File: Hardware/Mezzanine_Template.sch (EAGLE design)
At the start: 10 parts, among them U2 EDISON_CONNECTOR_FULLMOUNTING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, U3 EDISON_CONNECTOR_FULLHEADER

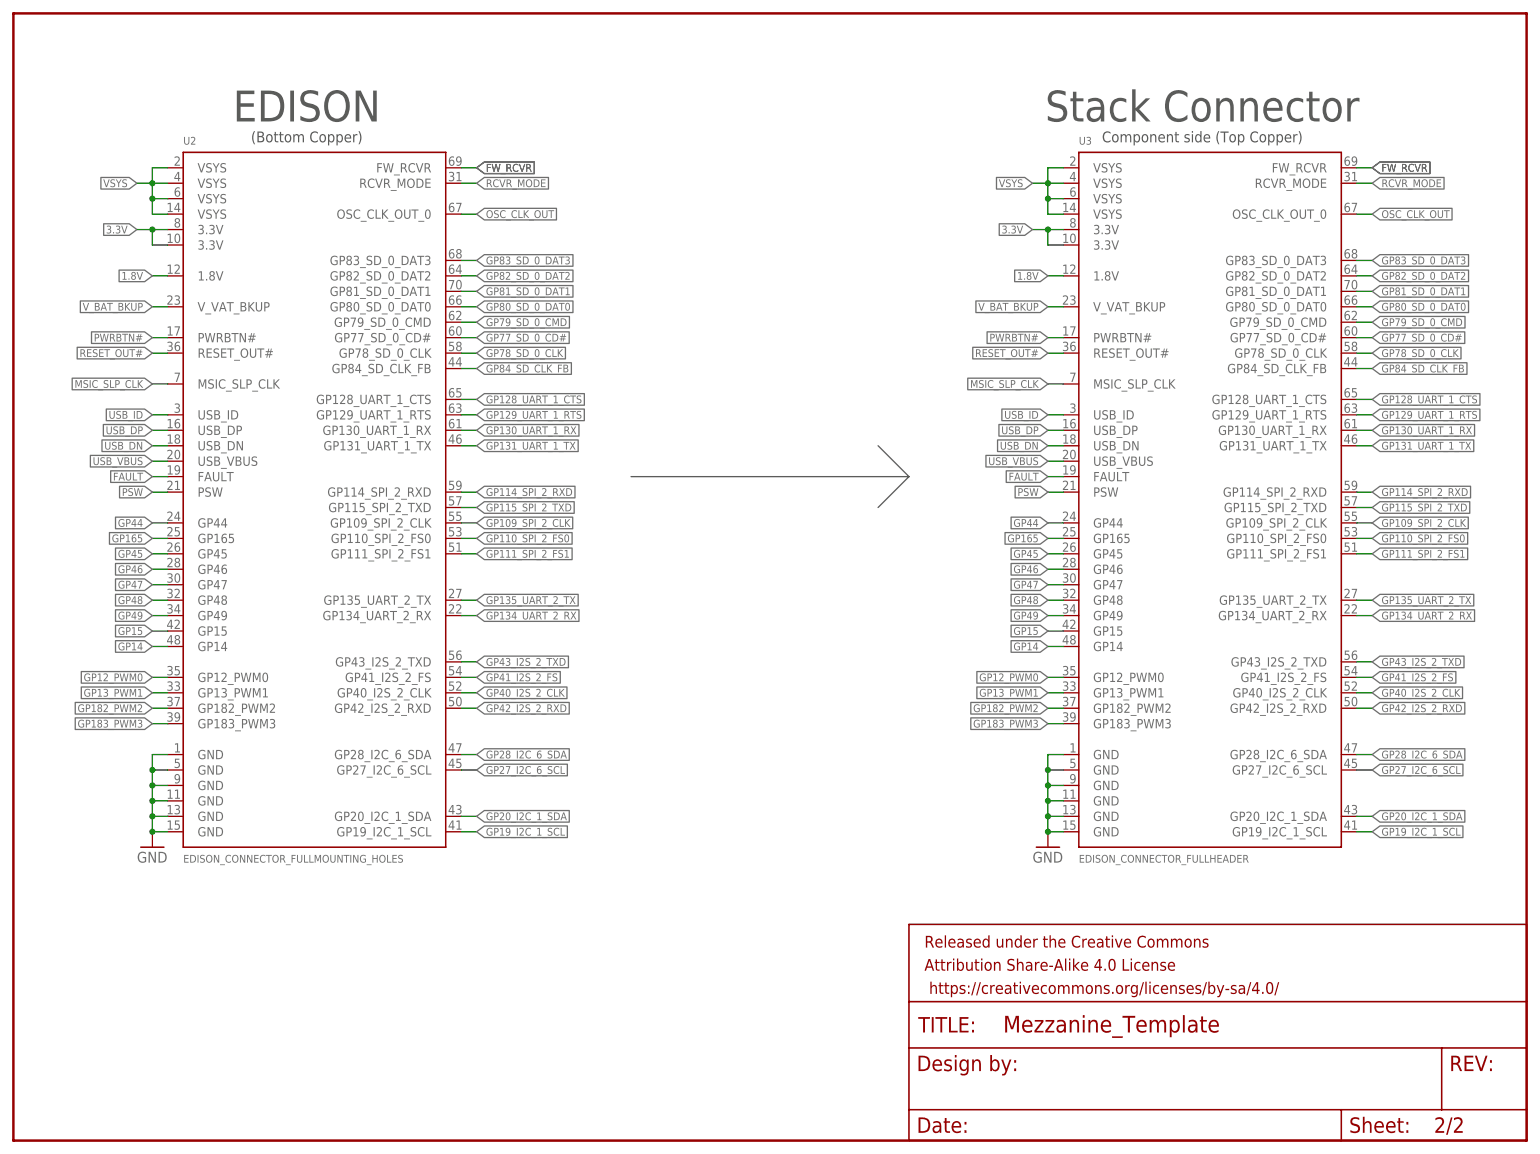
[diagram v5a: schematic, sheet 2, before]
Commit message: clean-up
Board
- Removed duplicate CC frame
- Adjusted sizes, ratios of text so they can be read when "Always Vector
Font" is set
- Adjusted positioning and alignment of text for consistency throughout
the drawing and making the text easier to edit (expansion)
- Fixed corner radius (indicated 0.08", should be 0.07")
- Added unit to the drill hole Dimension as it is -not- in inches
- Fixed top GND plane's bottom right corner (was off a smidgen)
- Centered the SparkFun logos (wiggle wiggle)
- Adjusted version number to 'v01.x' (not for release).  Please make
sure to adjust to appropriate version number before release!

Schematic
- Changed position, ratio and alignment of 'Engineer' in the frame to
align with the rest of the text and be consistent with the board
- Adjusted version number to 'v01.x' (not for release).  Please make
sure to adjust to appropriate version number before release!
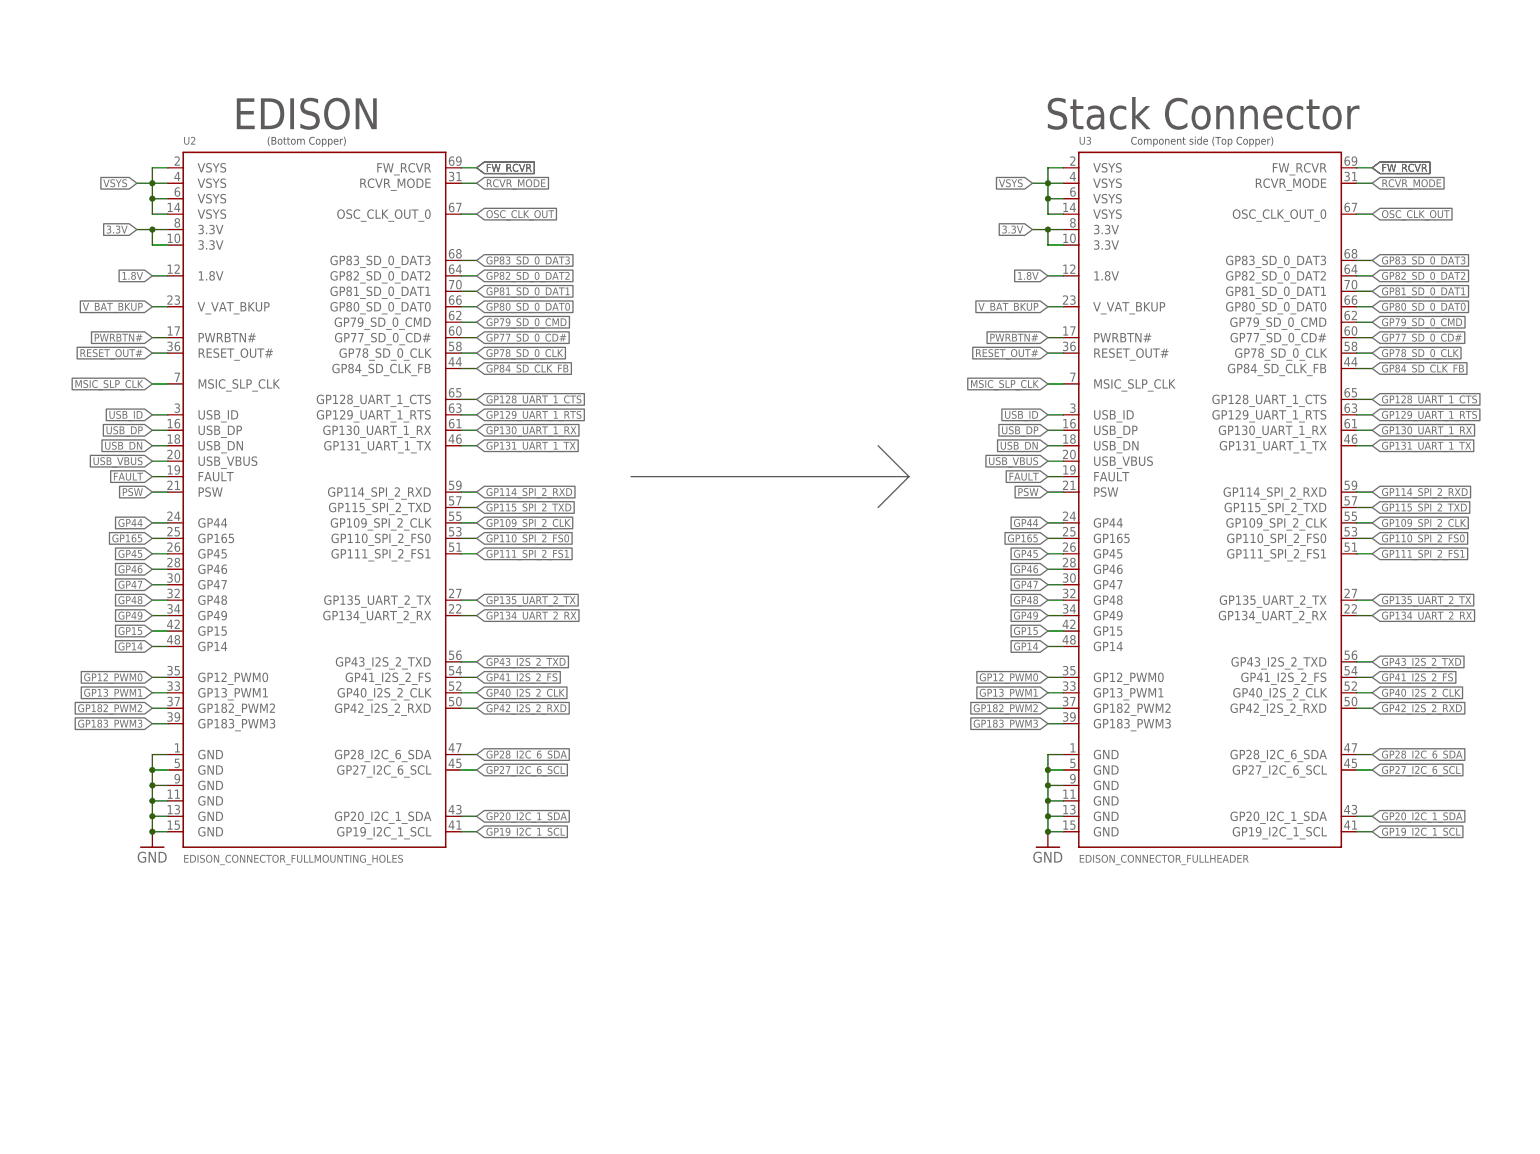
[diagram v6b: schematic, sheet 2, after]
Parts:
- removed FRAME2: FRAME-LETTER, SparkFun-Aesthetics:FRAME-LETTER
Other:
- note added: "v01.x"
- note removed: "v10"
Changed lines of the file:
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@@
 <?xml version="1.0" encoding="utf-8"?>
 <!DOCTYPE eagle SYSTEM "eagle.dtd">
-<eagle version="6.6.0">
+<eagle version="6.5.0">
 <drawing>
 <settings>
@@
 <part name="U3" library="Edison" deviceset="EDISON_CONNECTOR_FULL" device="HEADER" value="EDISON_CONNECTOR_FULLHEADER"/>
 <part name="GND4" library="supply1" deviceset="GND" device=""/>
-<part name="FRAME2" library="SparkFun-Aesthetics" deviceset="FRAME-LETTER" device=""/>
 <part name="FID1" library="SparkFun-Aesthetics" deviceset="FIDUCIAL" device="1X2"/>
 <part name="FID2" library="SparkFun-Aesthetics" deviceset="FIDUCIAL" device="1X2"/>
@@
 <sheet>
 <plain>
-<text x="238.76" y="7.62" size="2.54" layer="94">v10</text>
-<text x="167.64" y="10.16" size="2.54" layer="94">Engineer</text>
+<text x="236.22" y="7.62" size="2.54" layer="94" ratio="15">v01.x</text>
+<text x="172.72" y="13.97" size="2.54" layer="94" ratio="15" align="top-left">Engineer</text>
 </plain>
 <instances>
@@
 <sheet>
 <plain>
-<text x="48.26" y="170.18" size="5.08" layer="92" align="center">EDISON</text>
-<text x="195.58" y="170.18" size="5.08" layer="92" align="center">Stack Connector</text>
-<text x="195.58" y="165.1" size="1.778" layer="92" align="center">Component side (Top Copper)</text>
-<text x="48.26" y="165.1" size="1.778" layer="92" align="center">(Bottom Copper)</text>
+<text x="48.26" y="166.37" size="5.08" layer="92" align="bottom-center">EDISON</text>
+<text x="195.58" y="166.37" size="5.08" layer="92" align="bottom-center">Stack Connector</text>
+<text x="195.58" y="163.83" size="1.27" layer="92" align="bottom-center">Component side (Top Copper)</text>
+<text x="48.26" y="163.83" size="1.27" layer="92" align="bottom-center">(Bottom Copper)</text>
 </plain>
 <instances>
@@
 <instance part="U3" gate="G$1" x="177.8" y="132.08"/>
 <instance part="GND4" gate="1" x="170.18" y="48.26"/>
-<instance part="FRAME2" gate="G$1" x="0" y="0"/>
-<instance part="FRAME2" gate="G$2" x="147.32" y="0"/>
 </instances>
 <busses>

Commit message: replaced some changes made in pull request. updated git ignore to remover .epf
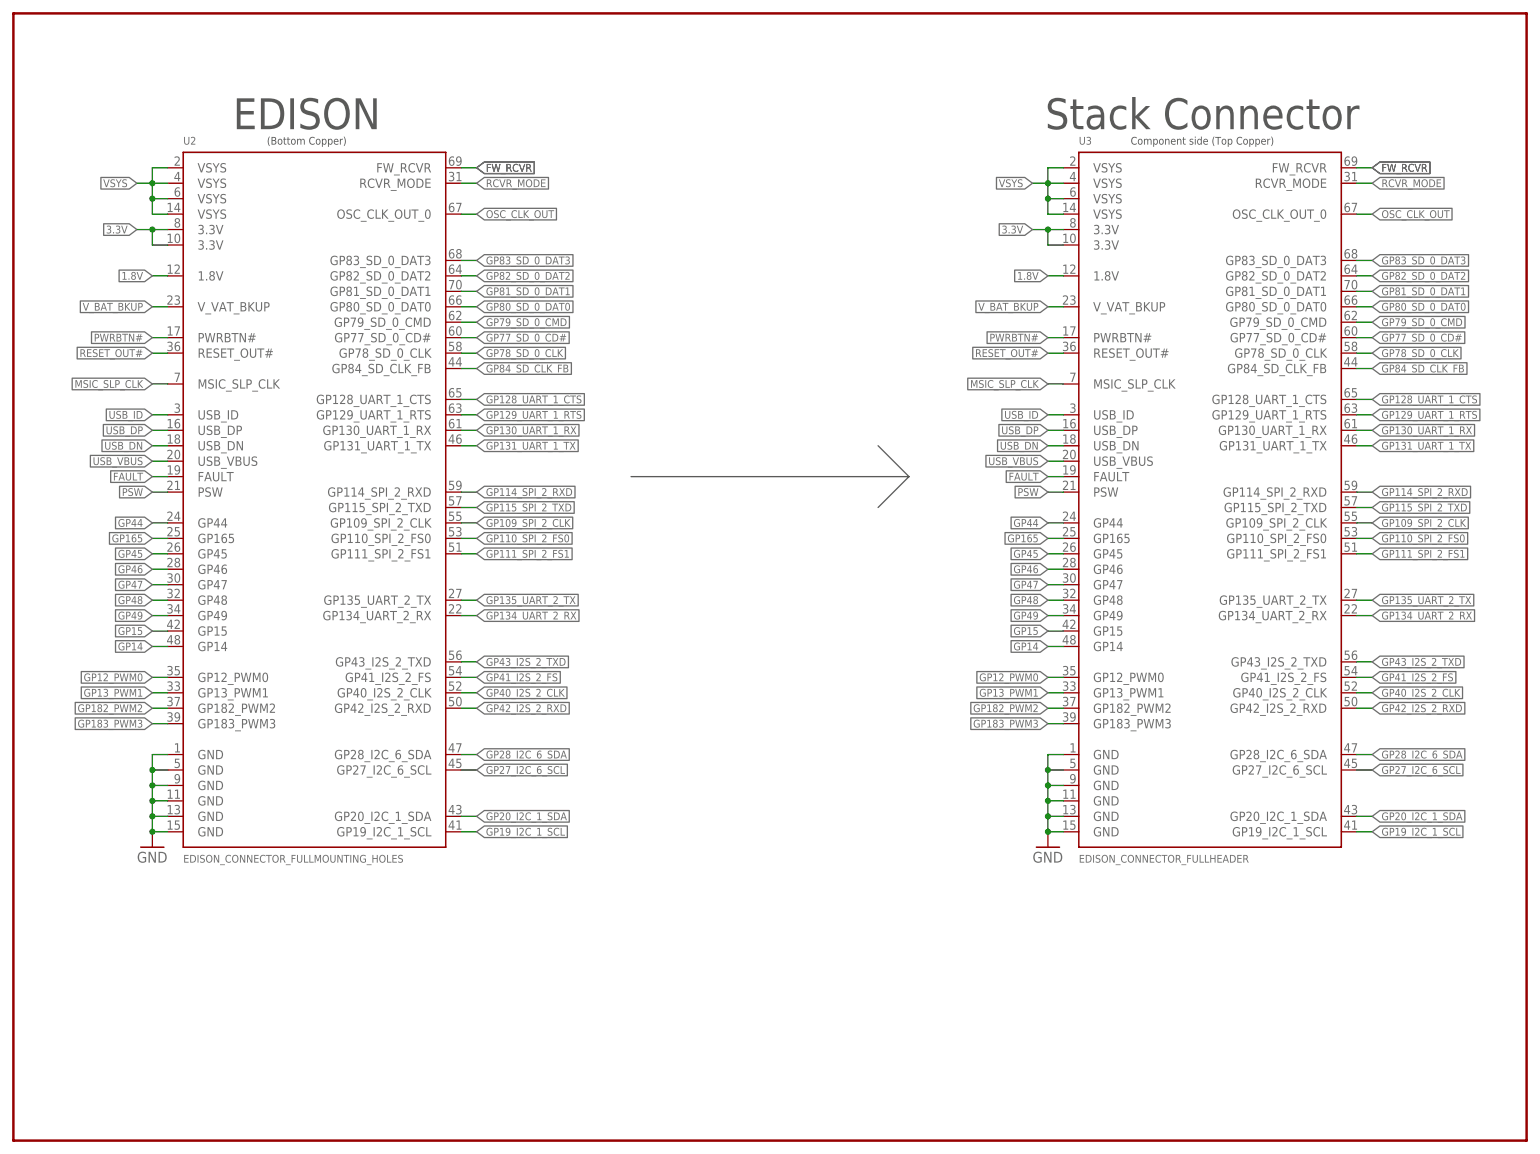
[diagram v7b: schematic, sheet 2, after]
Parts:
- added FRAME2: FRAME-LETTER, SparkFun-Aesthetics:FRAME-LETTER
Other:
- note added: "v01"
- note removed: "v01.x"
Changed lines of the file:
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@@
 <part name="FID3" library="SparkFun-Aesthetics" deviceset="FIDUCIAL" device="1X2"/>
 <part name="FID4" library="SparkFun-Aesthetics" deviceset="FIDUCIAL" device="1X2"/>
+<part name="FRAME2" library="SparkFun-Aesthetics" deviceset="FRAME-LETTER" device=""/>
 </parts>
 <sheets>
 <sheet>
 <plain>
-<text x="236.22" y="7.62" size="2.54" layer="94" ratio="15">v01.x</text>
+<text x="236.22" y="7.62" size="2.54" layer="94" ratio="15">v01</text>
 <text x="172.72" y="13.97" size="2.54" layer="94" ratio="15" align="top-left">Engineer</text>
 </plain>
@@
 <instance part="U3" gate="G$1" x="177.8" y="132.08"/>
 <instance part="GND4" gate="1" x="170.18" y="48.26"/>
+<instance part="FRAME2" gate="G$1" x="0" y="0"/>
 </instances>
 <busses>

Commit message: modified:   Hardware/Edison.lbr 	Corrected DCIN pin name on all schematic drawings
	modified:   Hardware/Mezzanine_Template.brd
	Re-positioned Vias to accomidate extra DCIN via
	Removed connection between VSYS and DCIN for boards
	that want to use battery monitoring features

	modified:   Hardware/Mezzanine_Template.sch
	Updated Schematic with current Lib Parts
	Added Note for DCIN pin usage.
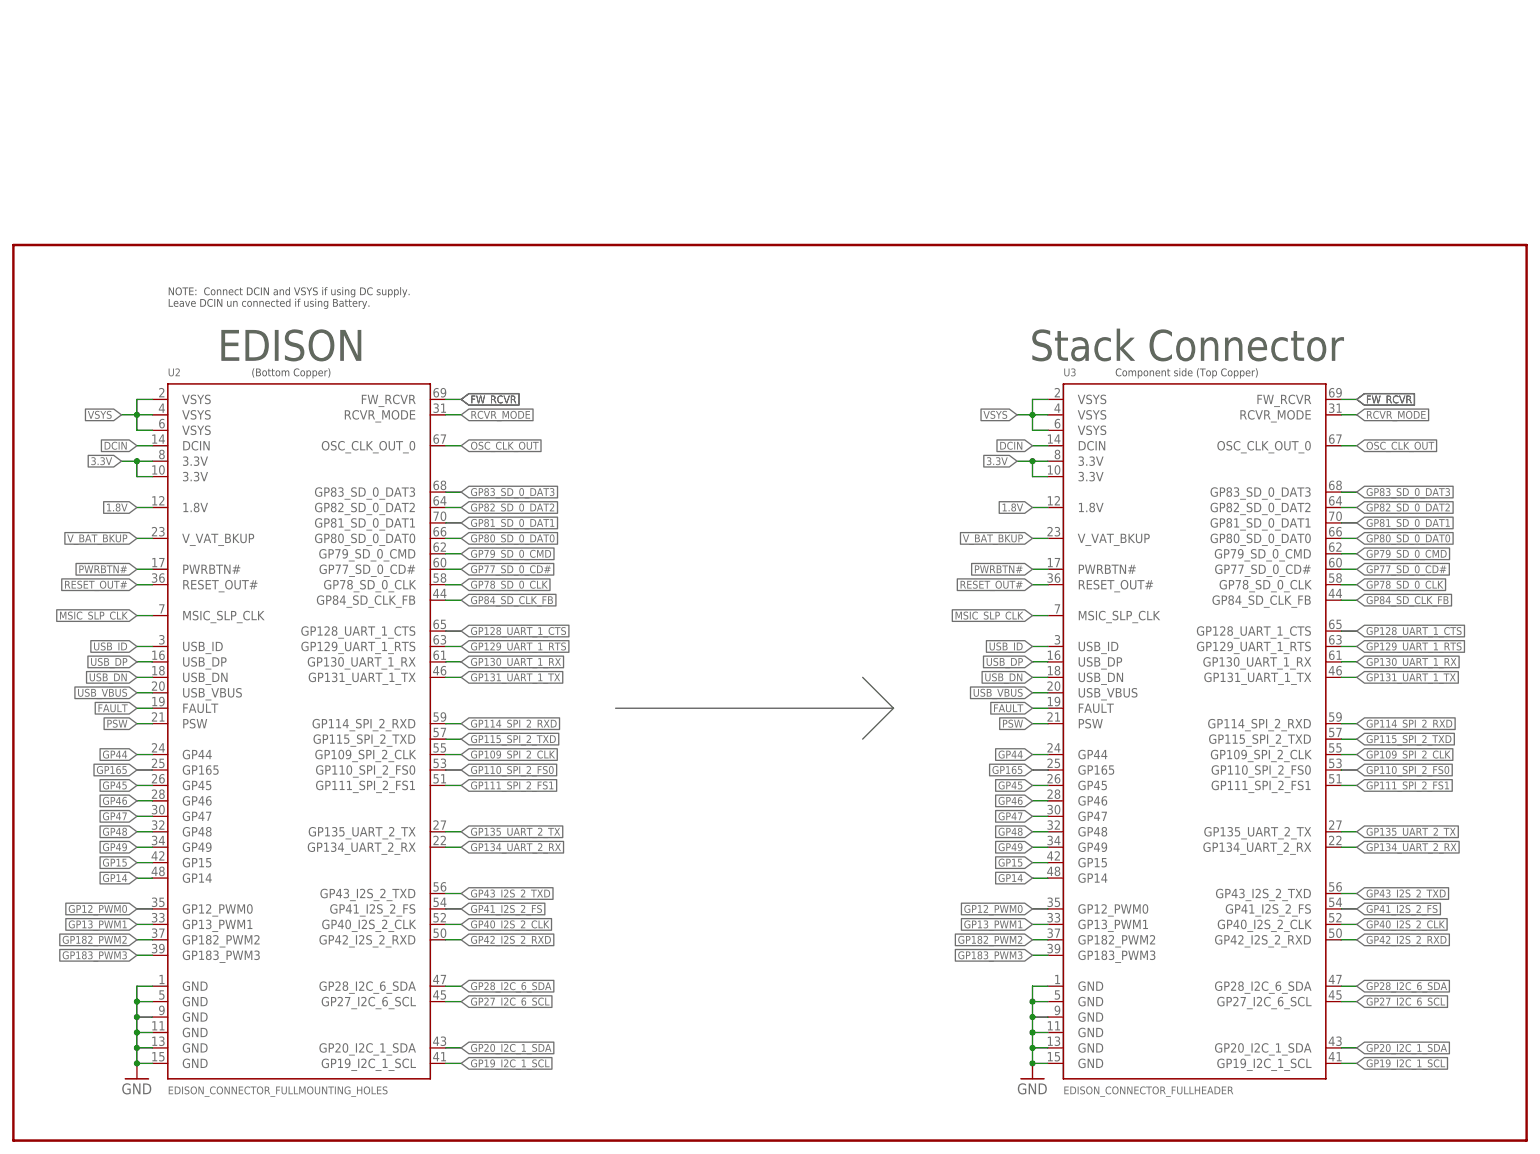
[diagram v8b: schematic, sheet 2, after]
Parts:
- removed FRAME2: FRAME-LETTER, SparkFun-Aesthetics:FRAME-LETTER
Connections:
- new net DCIN: U2.DCIN, U3.DCIN
- net VSYS: no longer U2.VSYS@4, U3.VSYS@4
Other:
- note added: "NOTE: Connect DCIN and VSYS if using DC supply. Leave DCIN un connected if using Battery."
- moved on the sheet: U2, U3
